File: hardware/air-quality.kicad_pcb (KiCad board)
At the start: 2 copper layers, 26 x 40 mm, 26 parts, among them J1 USB_C_Receptacle_USB2.0, Q1 UMH3N, U1 ME6211A33M3G-N, U2 CH340C, U3 ESP-12F, U4 SGP40, U5 HDC1080

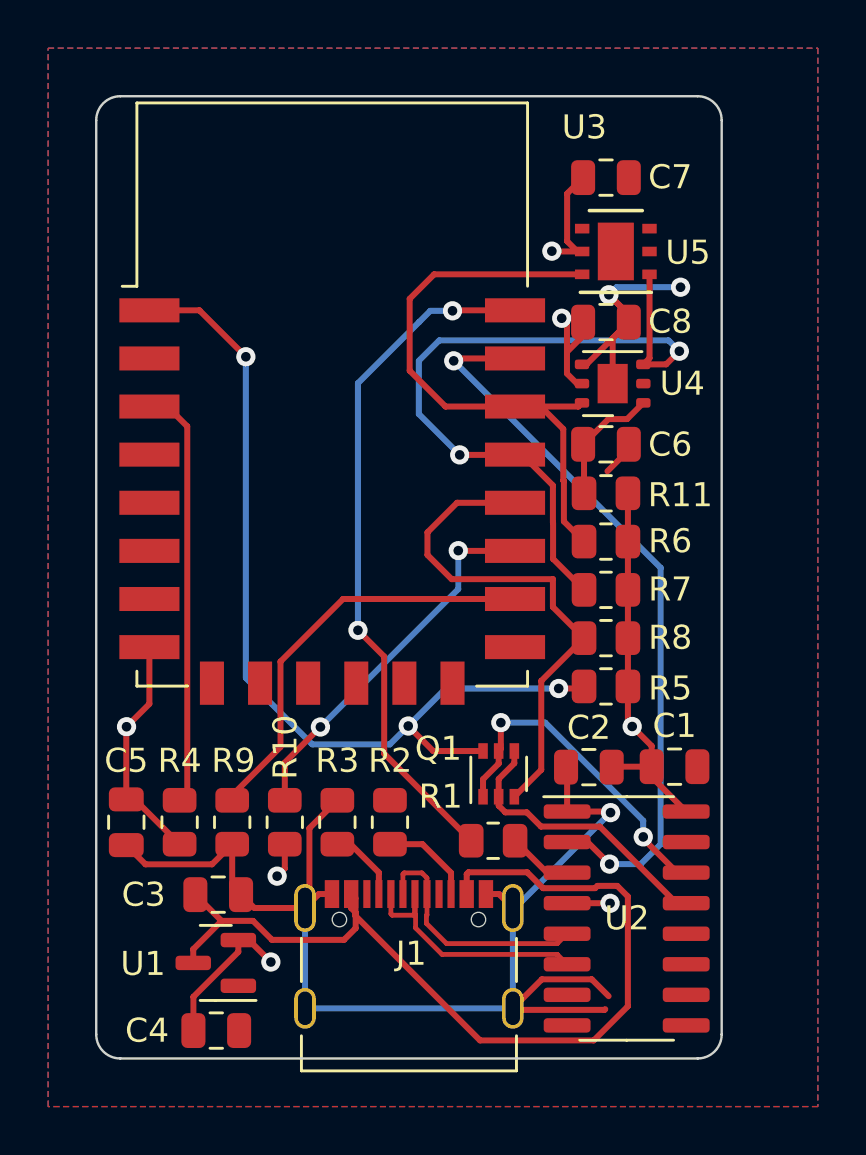
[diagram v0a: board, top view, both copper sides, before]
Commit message: Added display
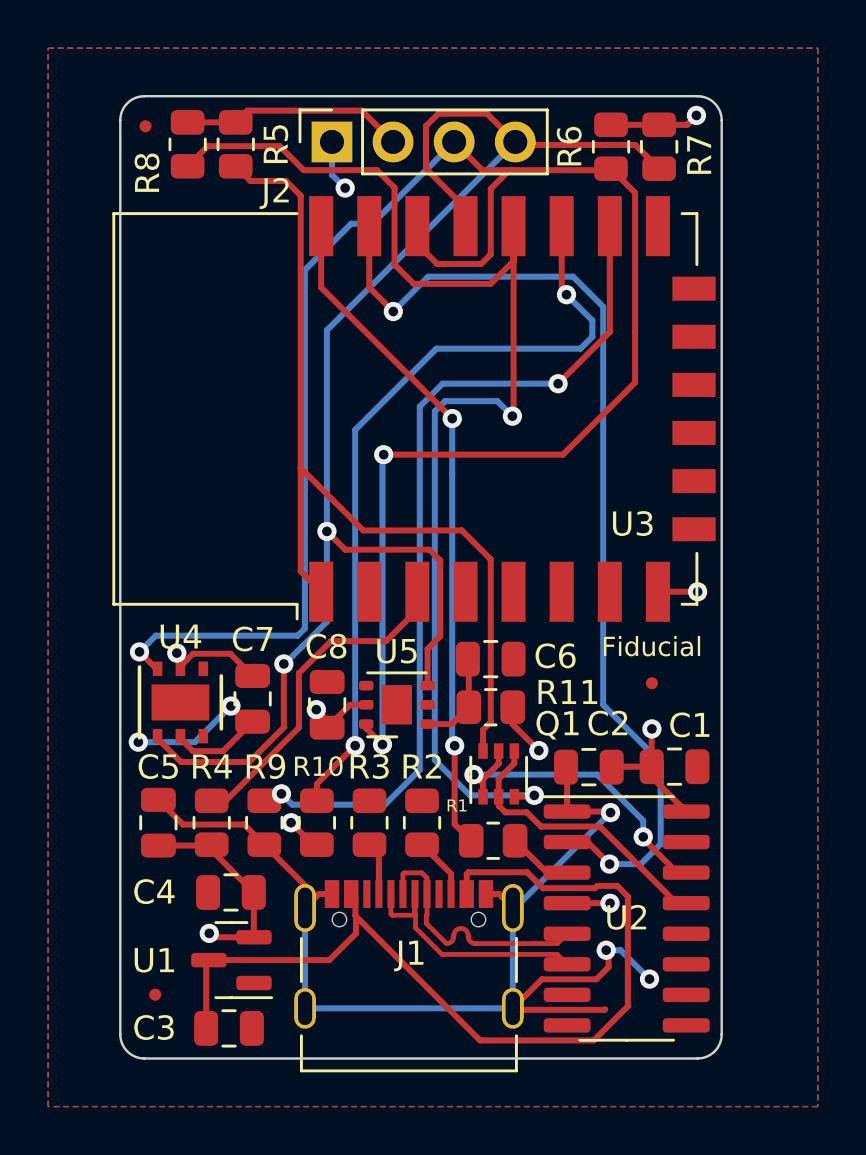
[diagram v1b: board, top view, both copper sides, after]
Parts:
- added FID1: Fiducial, Fiducial:Fiducial_0.5mm_Mask1mm, F.Cu at (122.5, 107.3)
- added FID2: Fiducial, Fiducial:Fiducial_0.5mm_Mask1mm, F.Cu at (143.1, 94.4)
- added FID3: Fiducial, Fiducial:Fiducial_0.5mm_Mask1mm, F.Cu at (122.0, 71.2)
- added G***: LOGO, LOGO, B.Cu at (133.0, 90.4)
- added J2: SSD1306, Connector_PinSocket_2.54mm:PinSocket_1x04_P2.54mm_Vertical, F.Cu at (129.8, 71.9)
- added REF**: KiCad-Logo2_5mm_SilkScreen, Symbol:KiCad-Logo2_5mm_SilkScreen, B.Cu at (133.8, 81.3)
- moved R5 27.3 mm to (125.8, 72.0), turned to -90 degrees
- moved R8 26.9 mm to (123.8, 72.0), turned to -90 degrees
- moved C7 26.2 mm to (126.5, 95.0), turned to -90 degrees
- moved U4 26.1 mm to (123.5, 95.2), turned to 90 degrees
- moved C8 19.7 mm to (129.6, 95.3), turned to 90 degrees
- moved R6 18.4 mm to (141.4, 72.1), turned to -90 degrees
- moved R7 16.6 mm to (143.4, 72.1), turned to -90 degrees
- moved U5 16.1 mm to (132.5, 95.3)
- moved C6 10.1 mm to (136.4, 93.4)
- moved R11 10.1 mm to (136.4, 95.4)
- moved C4 5.77 mm to (125.6, 103.1), turned to 180 degrees
- moved C3 5.58 mm to (125.5, 108.8)
- moved U3 3.10 mm to (132.8, 83.0), turned to 90 degrees
- moved C5 1.33 mm to (122.6, 100.2), turned to 90 degrees
- moved R10 1.33 mm to (129.2, 100.2)
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- renumbered R7 to R6, R6 to R7, U5 to U4, U4 to U5
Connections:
- R6 pad 2: /SDA -> /SCL
- R7 pad 2: /SCL -> /SDA
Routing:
- net /SCL: track 25.9 -> 81.1 mm, vias 0 -> 3
- net /SDA: track 30.8 -> 61.0 mm
- net /GPIO0: track 21.5 -> 51.7 mm, vias 0 -> 2
- net Net-(R9-Pad1): track 17.4 -> 36.4 mm, vias 0 -> 2
- net Net-(R10-Pad2): track 15.7 -> 32.7 mm
- net /RX: track 30.9 -> 41.7 mm
- net GND: track 66.1 -> 60.8 mm, vias 3 -> 6
- net +3V3: track 45.8 -> 41.9 mm, vias 7 -> 9
- net Net-(R4-Pad2): track 17.6 -> 13.9 mm
- net Net-(J1-PadB5): track 3.92 -> 2.55 mm
- net Net-(C6-Pad1): track 5.27 -> 4.02 mm
- net VBUS: track 39.0 -> 37.9 mm
- net Net-(J1-PadA5): track 3.11 -> 2.21 mm
- net /USB_DP: track 10.2 -> 10.9 mm
- net /TX: track 28.8 -> 28.1 mm
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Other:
- board size 26 x 40 mm -> 25 x 40 mm
- board text added: "Fiducial"
